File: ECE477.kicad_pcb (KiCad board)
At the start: 2 copper layers, 63 parts, among them IC2 ST1L05CPU33R, IC3 ST1L05BPUR, IC5 BQ29330DBT, J1 P7805-2000-S, Q1 NPN SOT23, Q2 NPN SOT23, Q3 NPN SOT23, Q4 NPN SOT23, U1 STM32H7_LQFP144_T2

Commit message: FIxing issues with the schematic import that I did not notice
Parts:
- removed C1, C28, C30: 4.7uF, Capacitor_SMD:C_0805_2012Metric_Pad1.15x1.40mm_HandSolder
- removed C10, C11, C12, C13, C14, C15, C17, C19, C2, C24, C25, C26, C27, C29, C3, C31, C32, C33, C4, C5, C6, C7, C8, C9: 100nF, Capacitor_SMD:C_0805_2012Metric_Pad1.15x1.40mm_HandSolder
- removed C16, C18: 1uF, Capacitor_SMD:C_0805_2012Metric_Pad1.15x1.40mm_HandSolder
- removed C20, C21, C23, C34, C35: 10uF, Capacitor_SMD:C_0805_2012Metric_Pad1.15x1.40mm_HandSolder
- removed C22: 220pF, Capacitor_SMD:C_0805_2012Metric_Pad1.15x1.40mm_HandSolder
- removed C36: 22uF, Capacitor_SMD:C_0805_2012Metric_Pad1.15x1.40mm_HandSolder
- removed IC2: ST1L05CPU33R, SamacSys_Parts:SON95P300X300X100-7N-D
- removed IC3: ST1L05BPUR, SamacSys_Parts:SON95P300X300X100-7N-D
- removed IC5: BQ29330DBT, SamacSys_Parts:SOP50P640X120-30N
- removed J1: P7805-2000-S, SamacSys_Parts:P78052000S
- removed JP1: Jumper_3_Open, Jumper:SolderJumper-3_P1.3mm_Open_Pad1.0x1.5mm
- removed L1: 2.2uH, 1.2A, Inductor_SMD:L_0805_2012Metric_Pad1.15x1.40mm_HandSolder
- removed L2: 22uH, Inductor_SMD:L_0805_2012Metric_Pad1.15x1.40mm_HandSolder
- removed Q1, Q2, Q3, Q4: NPN SOT23, digikey-footprints:SOT-23-3
- removed R1, R11, R2: 0R, Resistor_SMD:R_0805_2012Metric_Pad1.15x1.40mm_HandSolder
- removed R10, R5, R6, R9: 100K, Resistor_SMD:R_0805_2012Metric_Pad1.15x1.40mm_HandSolder
- removed R12, R13: 10K, Resistor_SMD:R_0805_2012Metric_Pad1.15x1.40mm_HandSolder
- removed R14: 56k, Resistor_SMD:R_0805_2012Metric_Pad1.15x1.40mm_HandSolder
- removed R15: 27k, Resistor_SMD:R_0805_2012Metric_Pad1.15x1.40mm_HandSolder
- removed R3, R4, R7, R8: 47K, Resistor_SMD:R_0805_2012Metric_Pad1.15x1.40mm_HandSolder
- removed U1: STM32H7_LQFP144_T2, STM_footprints:STM32H7_LQFP144_T2

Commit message: Added Pinout
Added footprints and pinout connections
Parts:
- added C1: 4.7uF, Capacitor_SMD:C_0805_2012Metric_Pad1.15x1.40mm_HandSolder, F.Cu at (81.3, 78.7)
- added C10: 100nF, Capacitor_SMD:C_0805_2012Metric_Pad1.15x1.40mm_HandSolder, F.Cu at (76.5, 78.7)
- added C11: 100nF, Capacitor_SMD:C_0805_2012Metric_Pad1.15x1.40mm_HandSolder, F.Cu at (133.4, 50.4)
- added C12: 100nF, Capacitor_SMD:C_0805_2012Metric_Pad1.15x1.40mm_HandSolder, F.Cu at (67.0, 79.6)
- added C13: 100nF, Capacitor_SMD:C_0805_2012Metric_Pad1.15x1.40mm_HandSolder, F.Cu at (148.0, 66.1)
- added C14: 100nF, Capacitor_SMD:C_0805_2012Metric_Pad1.15x1.40mm_HandSolder, F.Cu at (86.9, 75.8)
- added C15: 100nF, Capacitor_SMD:C_0805_2012Metric_Pad1.15x1.40mm_HandSolder, F.Cu at (120.9, 82.2)
- added C16: 1uF, Capacitor_SMD:C_0805_2012Metric_Pad1.15x1.40mm_HandSolder, F.Cu at (86.0, 78.7)
- added C17: 100nF, Capacitor_SMD:C_0805_2012Metric_Pad1.15x1.40mm_HandSolder, F.Cu at (148.0, 69.0)
- added C18: 1uF, Capacitor_SMD:C_0805_2012Metric_Pad1.15x1.40mm_HandSolder, F.Cu at (152.1, 52.9)
- added C19: 100nF, Capacitor_SMD:C_0805_2012Metric_Pad1.15x1.40mm_HandSolder, F.Cu at (133.4, 57.1)
- added C2: 100nF, Capacitor_SMD:C_0805_2012Metric_Pad1.15x1.40mm_HandSolder, F.Cu at (135.6, 79.5)
- added C20: 10uF, Capacitor_SMD:C_0805_2012Metric_Pad1.15x1.40mm_HandSolder, F.Cu at (143.4, 45.6)
- added C21: 10uF, Capacitor_SMD:C_0805_2012Metric_Pad1.15x1.40mm_HandSolder, F.Cu at (126.1, 79.3)
- added C22: 220pF, Capacitor_SMD:C_0805_2012Metric_Pad1.15x1.40mm_HandSolder, F.Cu at (162.6, 65.2)
- added C23: 10uF, Capacitor_SMD:C_0805_2012Metric_Pad1.15x1.40mm_HandSolder, F.Cu at (170.2, 73.2)
- added C24: 100nF, Capacitor_SMD:C_0805_2012Metric_Pad1.15x1.40mm_HandSolder, F.Cu at (142.0, 50.8)
- added C25: 100nF, Capacitor_SMD:C_0805_2012Metric_Pad1.15x1.40mm_HandSolder, F.Cu at (138.1, 57.1)
- added C26: 100nF, Capacitor_SMD:C_0805_2012Metric_Pad1.15x1.40mm_HandSolder, F.Cu at (153.1, 80.8)
- added C27: 100nF, Capacitor_SMD:C_0805_2012Metric_Pad1.15x1.40mm_HandSolder, F.Cu at (125.6, 82.2)
- added C28: 10uF, Capacitor_SMD:C_0805_2012Metric_Pad1.15x1.40mm_HandSolder, F.Cu at (110.5, 22.9)
- added C28: 4.7uF, Capacitor_SMD:C_0805_2012Metric_Pad1.15x1.40mm_HandSolder, F.Cu at (175.3, 37.9)
- added C29: 10uF, Capacitor_SMD:C_0805_2012Metric_Pad1.15x1.40mm_HandSolder, F.Cu at (123.1, 22.7)
- added C29: 100nF, Capacitor_SMD:C_0805_2012Metric_Pad1.15x1.40mm_HandSolder, F.Cu at (175.3, 30.2)
- added C3: 100nF, Capacitor_SMD:C_0805_2012Metric_Pad1.15x1.40mm_HandSolder, F.Cu at (124.7, 85.2)
- added C30: .1uF, Capacitor_SMD:C_0805_2012Metric_Pad1.15x1.40mm_HandSolder, F.Cu at (115.2, 22.9)
- added C30: 4.7uF, Capacitor_SMD:C_0805_2012Metric_Pad1.15x1.40mm_HandSolder, F.Cu at (189.2, 30.5)
- added C34: 10uF, Capacitor_SMD:C_0805_2012Metric_Pad1.15x1.40mm_HandSolder, F.Cu at (167.3, 65.2)
- added C35: 10uF, Capacitor_SMD:C_0805_2012Metric_Pad1.15x1.40mm_HandSolder, F.Cu at (156.8, 54.1)
- added C36: 22uF, Capacitor_SMD:C_0805_2012Metric_Pad1.15x1.40mm_HandSolder, F.Cu at (120.0, 85.2)
- added C4: 100nF, Capacitor_SMD:C_0805_2012Metric_Pad1.15x1.40mm_HandSolder, F.Cu at (72.7, 75.8)
- added C5: 100nF, Capacitor_SMD:C_0805_2012Metric_Pad1.15x1.40mm_HandSolder, F.Cu at (121.3, 79.3)
- added C6: 100nF, Capacitor_SMD:C_0805_2012Metric_Pad1.15x1.40mm_HandSolder, F.Cu at (71.8, 79.6)
- added C7: 100nF, Capacitor_SMD:C_0805_2012Metric_Pad1.15x1.40mm_HandSolder, F.Cu at (77.4, 75.8)
- added C8: 100nF, Capacitor_SMD:C_0805_2012Metric_Pad1.15x1.40mm_HandSolder, F.Cu at (138.7, 45.6)
- added C9: 100nF, Capacitor_SMD:C_0805_2012Metric_Pad1.15x1.40mm_HandSolder, F.Cu at (82.2, 75.8)
- added IC1: LP3852EMP-3.3_NOPB, SamacSys_Parts:SOT150P700X180-5N, F.Cu at (115.9, 17.3)
- added IC2: ST1L05CPU33R, SamacSys_Parts:SON95P300X300X100-7N-D, F.Cu at (182.9, 30.5)
- added IC5: BQ29330DBT, SamacSys_Parts:SOP50P640X120-30N, F.Cu at (120.8, 61.7)
- added J1: P7805-2000-S, SamacSys_Parts:P78052000S, F.Cu at (207.0, 24.1)
- added J2: Conn_01x05_Male, Connector_PinHeader_1.00mm:PinHeader_1x06_P1.00mm_Vertical, F.Cu at (122.4, 14.7)
- added J3: Conn_01x05_Male, Connector_PinHeader_1.00mm:PinHeader_1x05_P1.00mm_Vertical, F.Cu at (103.1, 22.4)
- added J4: Conn_01x05_Male, Connector_PinHeader_1.00mm:PinHeader_1x05_P1.00mm_Vertical, F.Cu at (106.4, 22.4)
- added JP1: Jumper_3_Open, Jumper:SolderJumper-3_P1.3mm_Open_Pad1.0x1.5mm, F.Cu at (67.5, 76.1)
- added L1: 2.2uH, 1.2A, Inductor_SMD:L_0805_2012Metric_Pad1.15x1.40mm_HandSolder, F.Cu at (130.4, 82.2)
- added L2: 22uH, Inductor_SMD:L_0805_2012Metric_Pad1.15x1.40mm_HandSolder, F.Cu at (142.9, 58.3)
- added R1: 0R, Resistor_SMD:R_0805_2012Metric_Pad1.15x1.40mm_HandSolder, F.Cu at (158.4, 81.6)
- added R11: 0R, Resistor_SMD:R_0805_2012Metric_Pad1.15x1.40mm_HandSolder, F.Cu at (129.5, 85.2)
- added R12: 10K, Resistor_SMD:R_0805_2012Metric_Pad1.15x1.40mm_HandSolder, F.Cu at (115.2, 25.8)
- added R12: 10K, Resistor_SMD:R_0805_2012Metric_Pad1.15x1.40mm_HandSolder, F.Cu at (182.9, 25.4)
- added R13: 10K, Resistor_SMD:R_0805_2012Metric_Pad1.15x1.40mm_HandSolder, F.Cu at (124.7, 25.6)
- added R2: 0R, Resistor_SMD:R_0805_2012Metric_Pad1.15x1.40mm_HandSolder, F.Cu at (170.2, 76.1)
- added R3: 100k, Resistor_SMD:R_0805_2012Metric_Pad1.15x1.40mm_HandSolder, F.Cu at (110.5, 25.8)
- added R4: 100k, Resistor_SMD:R_0805_2012Metric_Pad1.15x1.40mm_HandSolder, F.Cu at (120.0, 25.6)
- added SW1: SW_Push_Dual, Button_Switch_THT:SW_TH_Tactile_Omron_B3F-10xx, F.Cu at (103.0, 14.8)
- added U1: STM32H7_LQFP144_T2, STM_footprints:STM32H7_LQFP144_T2, F.Cu at (74.9, 48.3)

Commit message: Updated post review with team members
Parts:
- added J5: Conn_01x05_Male, Connector_PinHeader_1.00mm:PinHeader_1x05_P1.00mm_Vertical, F.Cu at (63.5, 11.4)
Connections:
- net 1V8_VDD renamed OFF
- J3 pad 5: PWM5 -> Touch_Input

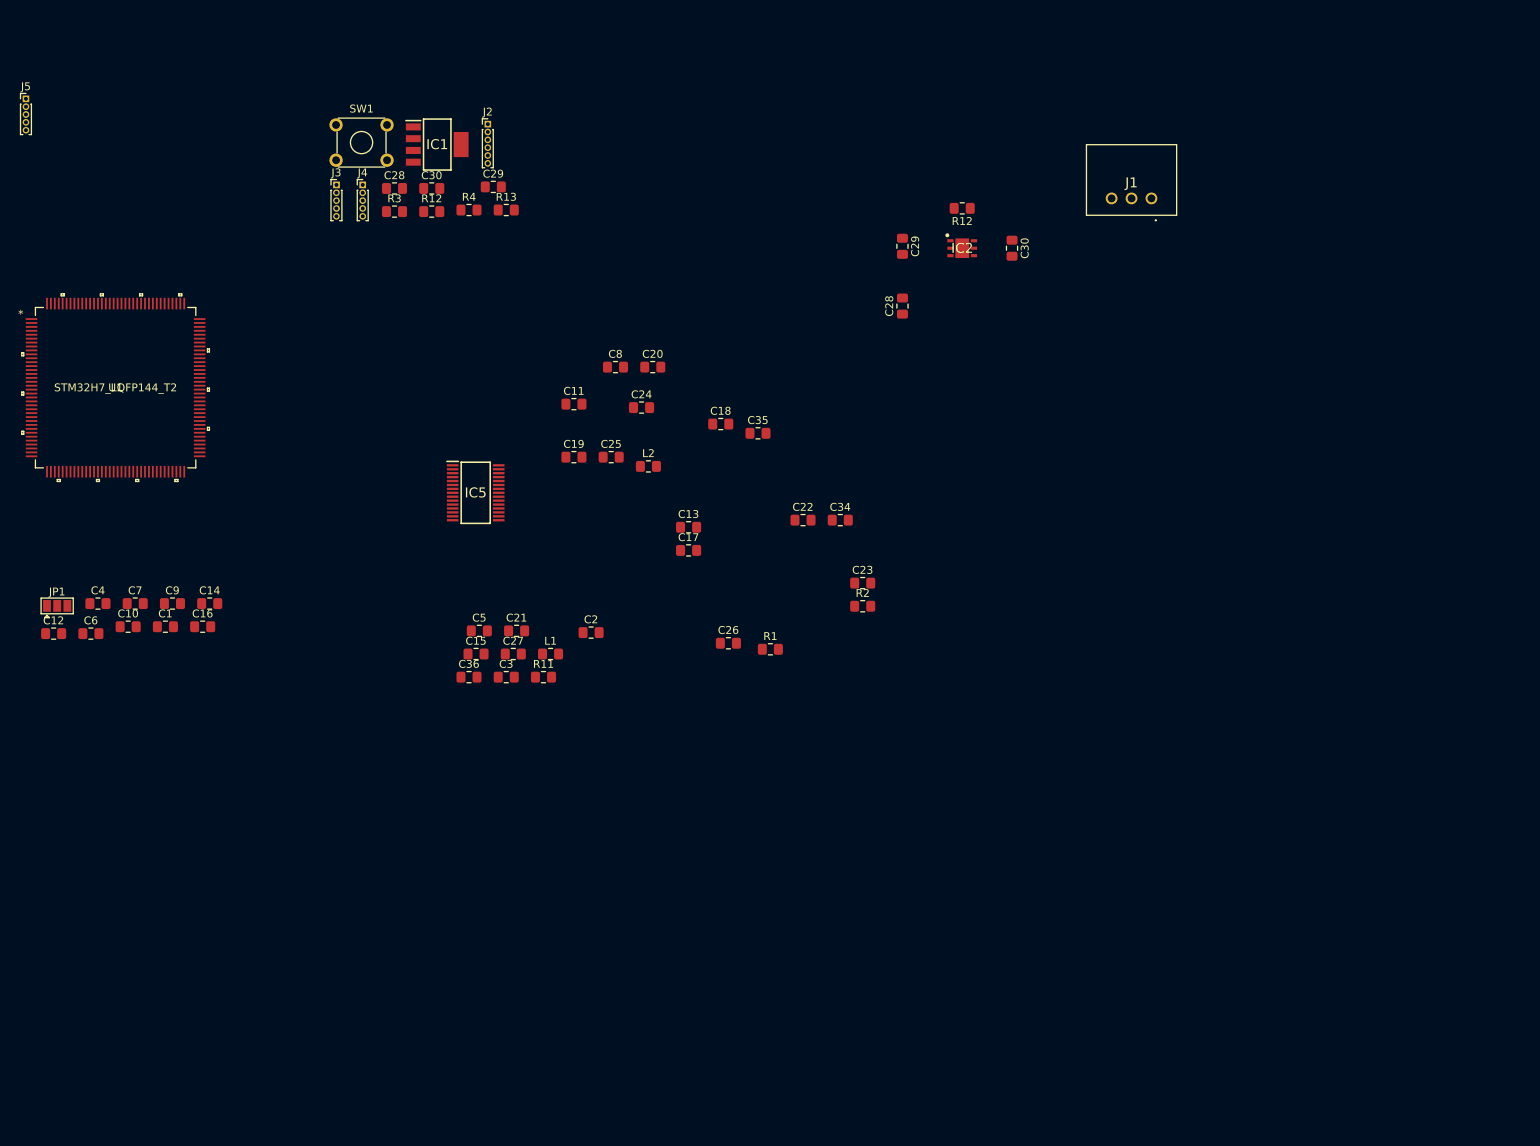
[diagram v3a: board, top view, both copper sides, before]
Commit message: Label and layout updates
Updated Labesl for simplicity along with a starting footprint layout for our PCB.
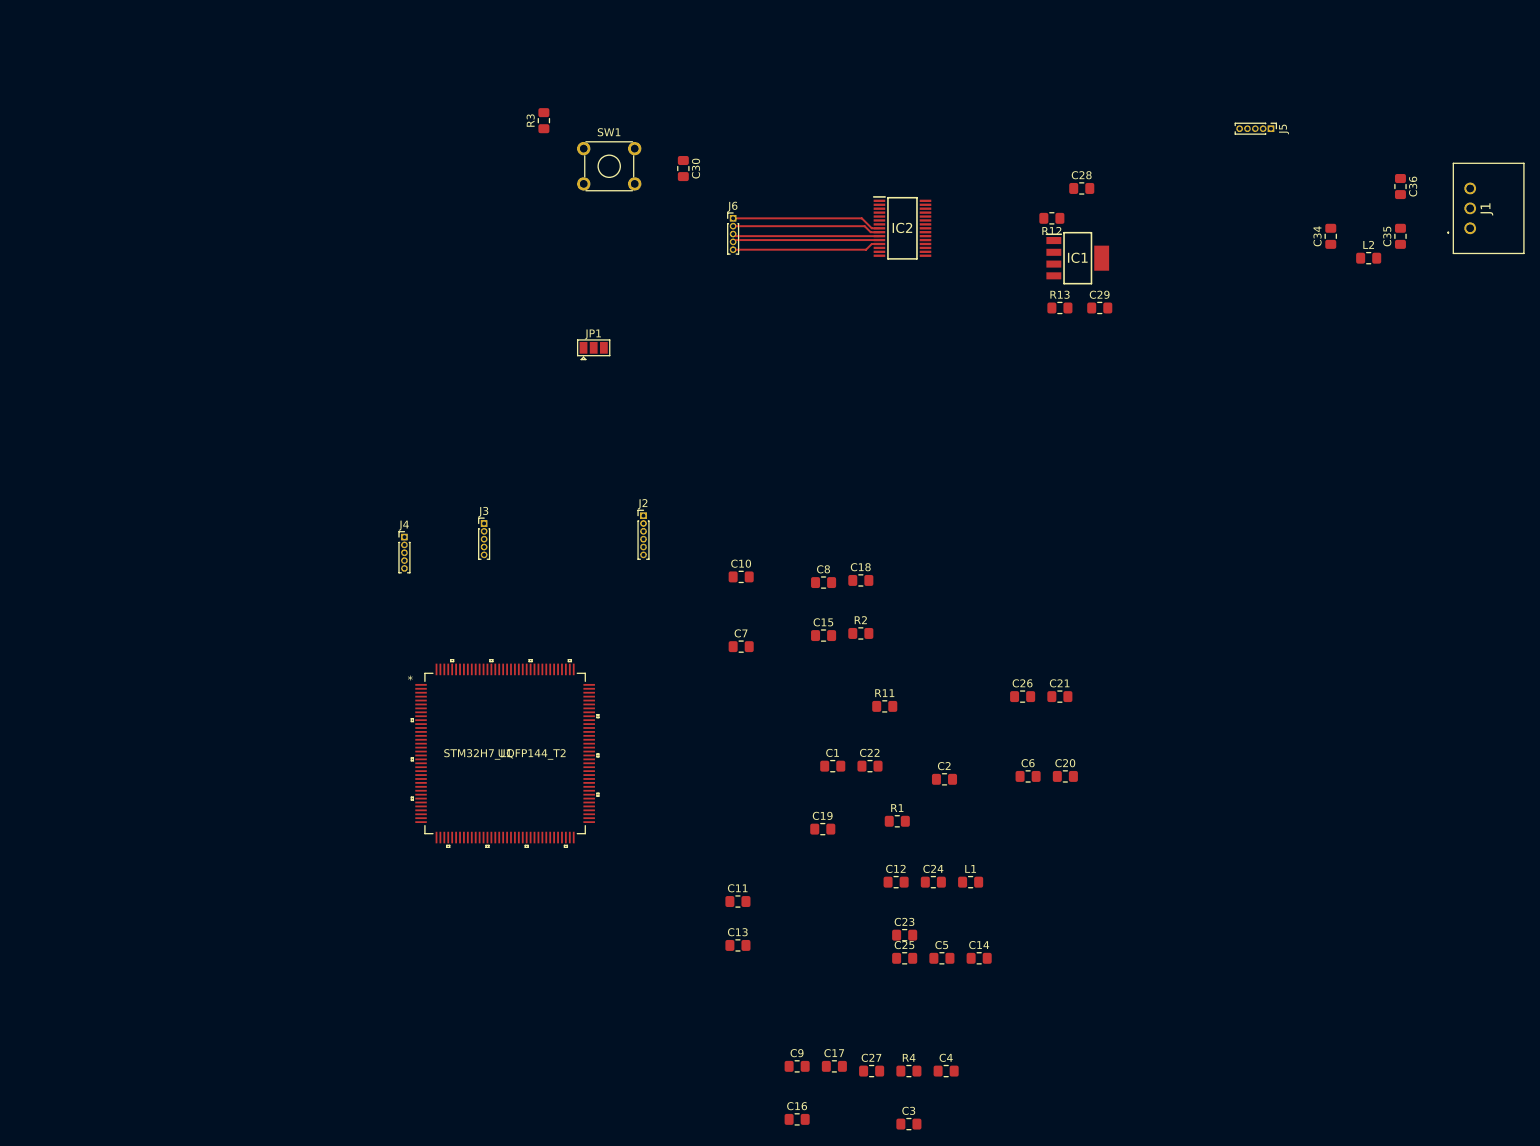
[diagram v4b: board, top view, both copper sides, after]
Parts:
- removed the C28 at (110.5, 22.9)
- removed the C28 at (175.3, 37.9)
- removed the C29 at (123.1, 22.7)
- removed the C29 at (175.3, 30.2)
- removed the C30 at (115.2, 22.9)
- removed the C30 at (189.2, 30.5)
- removed IC5: BQ29330DBT, SamacSys_Parts:SOP50P640X120-30N
- removed the R12 at (115.2, 25.8)
- removed the R12 at (182.9, 25.4)
- added C28: 10uF, Capacitor_SMD:C_0805_2012Metric_Pad1.15x1.40mm_HandSolder, F.Cu at (198.1, 22.9)
- added C29: 10uF, Capacitor_SMD:C_0805_2012Metric_Pad1.15x1.40mm_HandSolder, F.Cu at (200.4, 38.1)
- added C30: .1uF, Capacitor_SMD:C_0805_2012Metric_Pad1.15x1.40mm_HandSolder, F.Cu at (147.3, 20.3)
- added J6: Conn_01x05_Male, Connector_PinHeader_1.00mm:PinHeader_1x05_P1.00mm_Vertical, F.Cu at (153.7, 26.7)
- added R12: 10K, Resistor_SMD:R_0805_2012Metric_Pad1.15x1.40mm_HandSolder, F.Cu at (194.3, 26.7)
- IC2: value ST1L05CPU33R -> BQ29330DBT; footprint SamacSys_Parts:SON95P300X300X100-7N-D -> SamacSys_Parts:SOP50P640X120-30N
- moved J5 158.8 mm to (222.2, 15.2), turned to 270 degrees
- moved C36 134.2 mm to (238.8, 22.6), turned to 270 degrees
- moved C4 123.5 mm to (180.8, 135.4)
- moved R4 123.3 mm to (176.1, 135.4)
- moved C6 120.9 mm to (191.3, 97.8)
- moved C12 112.0 mm to (174.4, 111.3)
- moved C14 108.0 mm to (185.0, 121.0)
- moved C9 99.1 mm to (161.8, 134.8)
- moved C16 98.4 mm to (161.8, 141.6)
- moved L2 95.6 mm to (234.7, 31.8)
- moved C1 86.9 mm to (166.4, 96.5)
- moved C35 85.7 mm to (238.8, 29.0), turned to 90 degrees
- moved IC1 82.9 mm to (197.6, 31.8)
- moved C10 78.4 mm to (154.7, 72.4)
- moved C7 77.5 mm to (154.7, 81.3)
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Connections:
- C1 pad 1: VBAT -> VDDSMPS_IN
- C10 pad 1: VBAT -> VDDSMPS_IN
- C11 pad 1: VBAT -> VDDSMPS_IN
- C12 pad 1: VBAT -> VDDSMPS_IN
- C13 pad 1: VBAT -> VDDSMPS_IN
- C14 pad 1: VBAT -> VDDSMPS_IN
- C16 pad 2: GNDA -> GND
- C17 pad 2: GNDA -> GND
- C18 pad 2: GNDA -> GND
- C19 pad 2: GNDA -> GND
- C2 pad 1: VBAT -> VDDSMPS_IN
- C20 pad 1: VBAT -> VDDSMPS_IN
- C21 pad 1: VBAT -> VDDSMPS_IN
- C3 pad 1: VBAT -> VDDSMPS_IN
- C4 pad 1: VBAT -> VDDSMPS_IN
- C5 pad 1: VBAT -> VDDSMPS_IN
- C6 pad 1: VBAT -> VDDSMPS_IN
- C7 pad 1: VBAT -> VDDSMPS_IN
- C8 pad 1: VBAT -> VDDSMPS_IN
- C9 pad 1: VBAT -> VDDSMPS_IN
- IC2 pad 1: Net-(C29-Pad1) -> GND
- IC2 pad 2: GND -> PWR_IN
- IC2 pad 4: 3V3_PER -> Net-(IC2-Pad4)
- IC2 pad 5: 3V3_PER -> Net-(IC2-Pad5)
- IC2 pad 6: 5V -> Net-(IC2-Pad6)
- IC2 pad 7: GND -> Net-(IC2-Pad7)
- J3 pad 5: Touch_Input -> PWM5
- JP1 pad 2: VBAT -> VDDSMPS_IN
- R1 pad 1: VBAT -> VDDSMPS_IN
- R3 pad 2: VBAT -> VDDSMPS_IN
- U1 pad 106: VBAT -> VDDSMPS_IN
- U1 pad 119: VBAT -> VDDSMPS_IN
- U1 pad 129: VBAT -> VDDSMPS_IN
- U1 pad 13: VBAT -> VDDSMPS_IN
- U1 pad 144: VBAT -> VDDSMPS_IN
- U1 pad 16: VBAT -> VDDSMPS_IN
- U1 pad 19: VBAT -> VDDSMPS_IN
- U1 pad 32: VBAT -> VDDSMPS_IN
- U1 pad 34: GNDA -> GND
- U1 pad 42: VBAT -> VDDSMPS_IN
- U1 pad 56: VBAT -> VDDSMPS_IN
- U1 pad 7: VBAT -> VDDSMPS_IN
- U1 pad 71: VBAT -> VDDSMPS_IN
- U1 pad 79: VBAT -> VDDSMPS_IN
- U1 pad 8: VBAT -> VDDSMPS_IN
- U1 pad 92: VBAT -> VDDSMPS_IN
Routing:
- net V5: track 0.00 -> 19.2 mm
- net V4: track 0.00 -> 19.0 mm
- net V1: track 0.00 -> 19.0 mm
- net V3: track 0.00 -> 18.8 mm
- net V2: track 0.00 -> 18.7 mm
